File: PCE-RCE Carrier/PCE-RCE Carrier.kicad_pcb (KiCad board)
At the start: 2 copper layers, 38 x 39.5 mm, 52 parts, among them J1 TBL002A-350-08GY-2GY, J10 Conn_01x06_Pin, J11 XT30PW-M, J2 XT60PW-F, J4 XT60PW-F, J5 DF40C-34DP-0.4V_58_, J6 PRT-16766, J7 DF40C-34DP-0.4V_58_, J9 XT30PW-M, Q1 2SD2537, Q2 2SD2537, Q3 2SD2537, Q4 2SD2537, U1 TPS75533KTTRG3, U2 TPS54302DDCR, U3 BD6222HFP-TR, U4 LMR51430, U5 BD6222HFP-TR

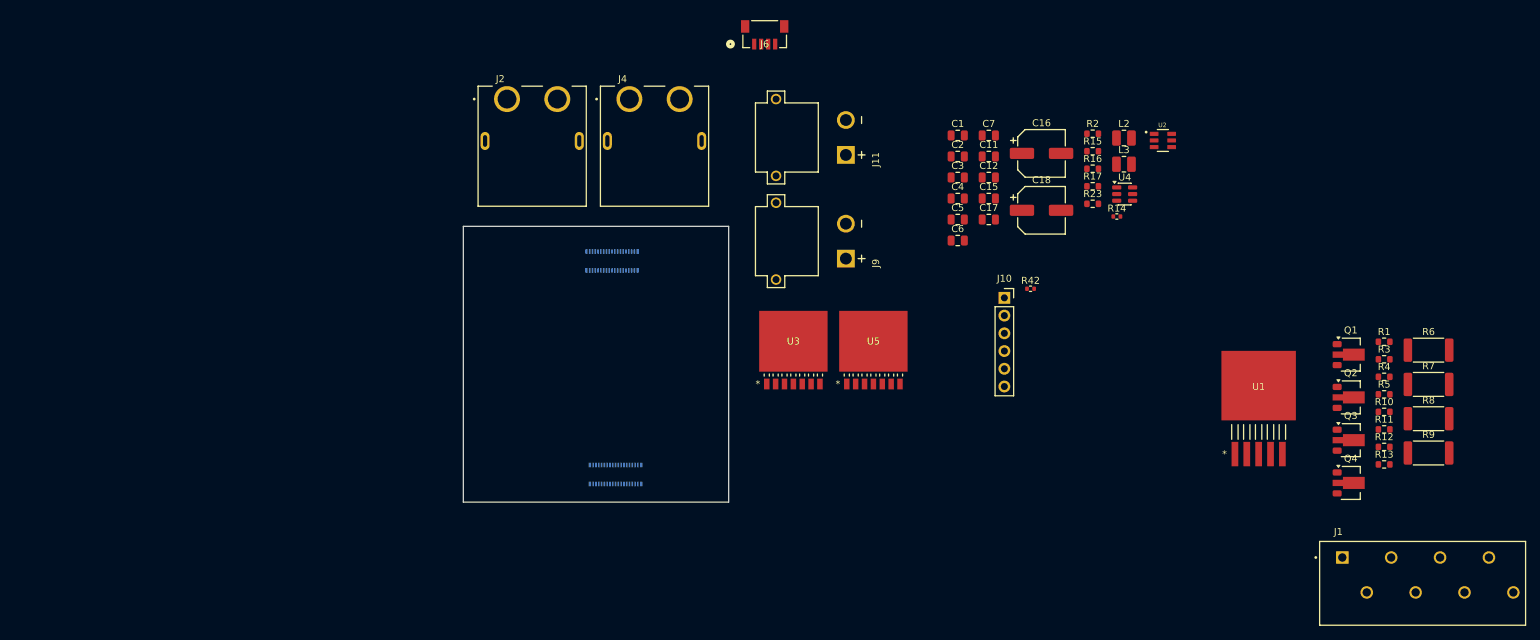
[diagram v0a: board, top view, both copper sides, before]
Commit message: mfw high power components are large
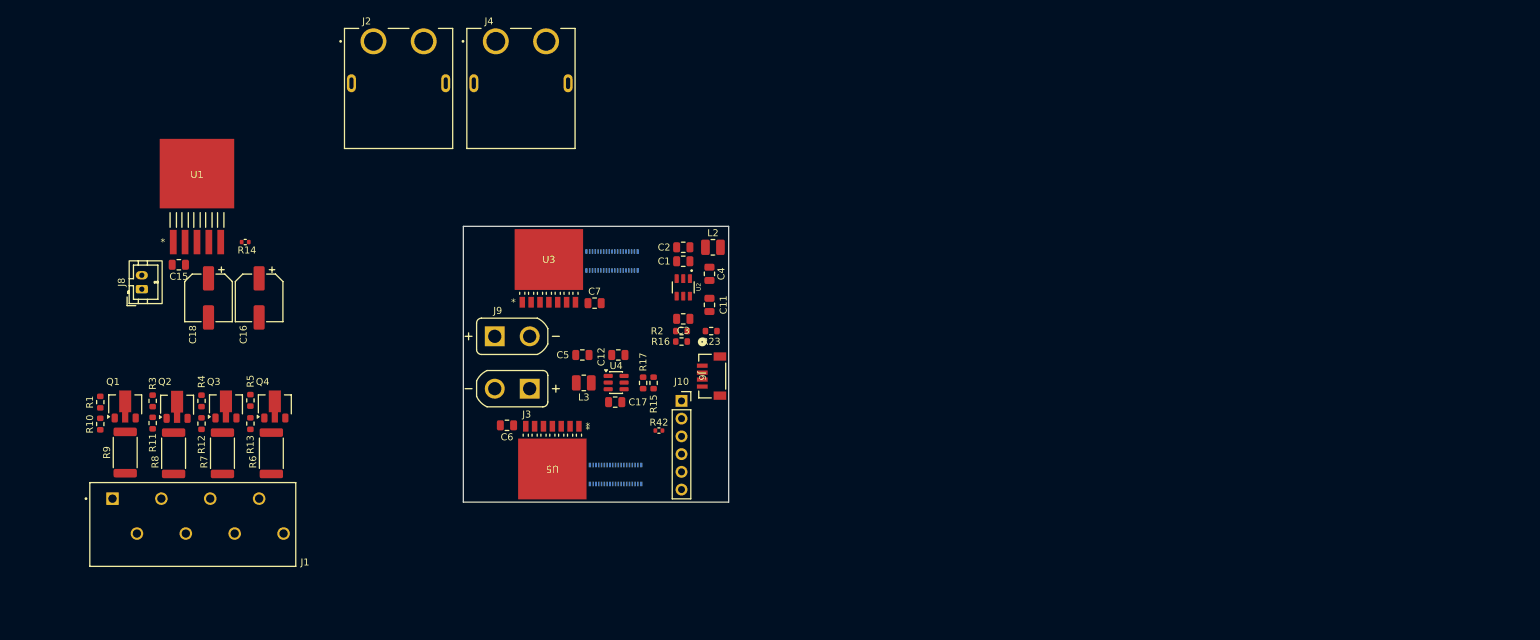
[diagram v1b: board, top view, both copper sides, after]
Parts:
- removed J11: XT30PW-M, XT30PW-M:AMASS_XT30PW-M
- added J3: XT30UPB-M, XT30UPB-M:AMASS_XT30UPB-M, F.Cu at (129.0, 77.2)
- added J8: Conn_01x02_Pin, Connector_JST:JST_PH_B2B-PH-K_1x02_P2.00mm_Vertical, F.Cu at (76.0, 63.0)
- J9: value XT30PW-M -> XT30UPB-M; footprint XT30PW-M:AMASS_XT30PW-M -> XT30UPB-M:AMASS_XT30UPB-M
- moved R9 186.7 mm to (73.6, 86.4), turned to 90 degrees
- moved R1 184.1 mm to (70.0, 79.2), turned to -90 degrees
- moved R10 183.9 mm to (70.0, 82.3), turned to -90 degrees
- moved R8 179.8 mm to (80.5, 86.5), turned to 90 degrees
- moved R3 176.5 mm to (77.5, 79.0), turned to -90 degrees
- moved R11 176.4 mm to (77.5, 82.2), turned to -90 degrees
- moved J1 176.3 mm to (71.8, 93.0)
- moved Q1 175.7 mm to (73.6, 79.5), turned to 90 degrees
- moved R7 173.0 mm to (87.5, 86.5), turned to 90 degrees
- moved R4 169.4 mm to (84.5, 79.0), turned to -90 degrees
- moved R12 169.4 mm to (84.5, 82.2), turned to -90 degrees
- moved Q2 168.1 mm to (81.0, 79.5), turned to 90 degrees
- moved R6 166.4 mm to (94.5, 86.5), turned to 90 degrees
- moved R13 162.5 mm to (91.5, 82.2), turned to -90 degrees
- moved R5 162.4 mm to (91.5, 78.9), turned to -90 degrees
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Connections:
- J10 pad 2: /MOSI -> Net-(J10-Pin_2)
- J10 pad 3: Net-(J10-Pin_3) -> /MOSI
- J9 pad N: /Power Distribution and Motor Control/MOTOR2B -> /Power Distribution and Motor Control/MOTOR1B
- J9 pad P: /Power Distribution and Motor Control/MOTOR2A -> /Power Distribution and Motor Control/MOTOR1A
- R42 pad 2: Net-(J10-Pin_3) -> Net-(J10-Pin_2)

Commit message: initial component placement can you feel the layout hell
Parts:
- moved J4 58.8 mm to (143.7, 84.8)
- moved R1 49.3 mm to (118.7, 87.4), turned to 90 degrees
- moved R10 48.7 mm to (118.7, 84.2), turned to 90 degrees
- moved J2 47.4 mm to (143.2, 63.8), turned to 180 degrees
- moved Q1 42.2 mm to (115.1, 87.0), turned to -90 degrees
- moved R9 42.0 mm to (115.1, 80.2), turned to -90 degrees
- moved R3 34.7 mm to (111.2, 87.5), turned to 90 degrees
- moved U1 34.7 mm to (115.8, 60.2), turned to -90 degrees
- moved R11 33.7 mm to (111.2, 84.4), turned to 90 degrees
- moved R8 28.4 mm to (108.2, 80.0), turned to -90 degrees
- moved Q2 27.7 mm to (107.7, 87.0), turned to -90 degrees
- moved C15 21.7 mm to (102.8, 57.6), turned to 90 degrees
- moved R4 21.4 mm to (104.2, 87.5), turned to 90 degrees
- moved R12 19.8 mm to (104.2, 84.3), turned to 90 degrees
- moved R14 18.8 mm to (106.1, 67.2), turned to 90 degrees
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
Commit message: potentially better placement that was revealed to me in my shower
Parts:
- moved C15 20.7 mm to (82.2, 58.1)
- moved C16 20.7 mm to (77.4, 69.6)
- moved C18 20.7 mm to (77.4, 62.4)
- moved J1 20.7 mm to (60.0, 90.0)
- moved J8 20.7 mm to (70.0, 57.8)
- moved Q1 20.7 mm to (94.4, 87.5)
- moved Q2 20.7 mm to (87.0, 87.5)
- moved Q3 20.7 mm to (80.0, 87.5)
- moved Q4 20.7 mm to (73.0, 87.5)
- moved R1 20.7 mm to (98.0, 87.9)
- moved R10 20.7 mm to (98.0, 84.7)
- moved R11 20.7 mm to (90.5, 84.9)
- moved R12 20.7 mm to (83.5, 84.8)
- moved R13 20.7 mm to (76.5, 84.8)
- moved R14 20.7 mm to (85.4, 67.7)
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
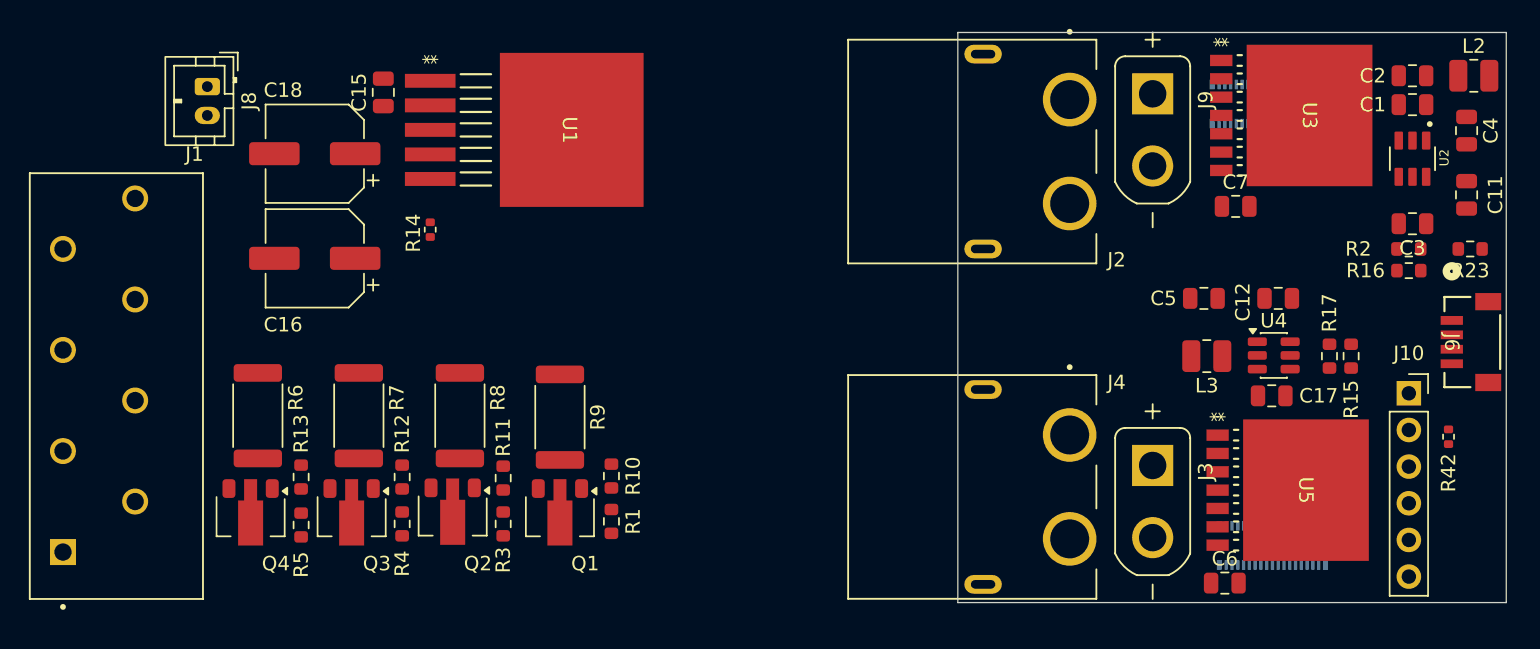
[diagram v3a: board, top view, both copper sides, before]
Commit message: some pce routing, switched out ace battery connectors for vertical xt30
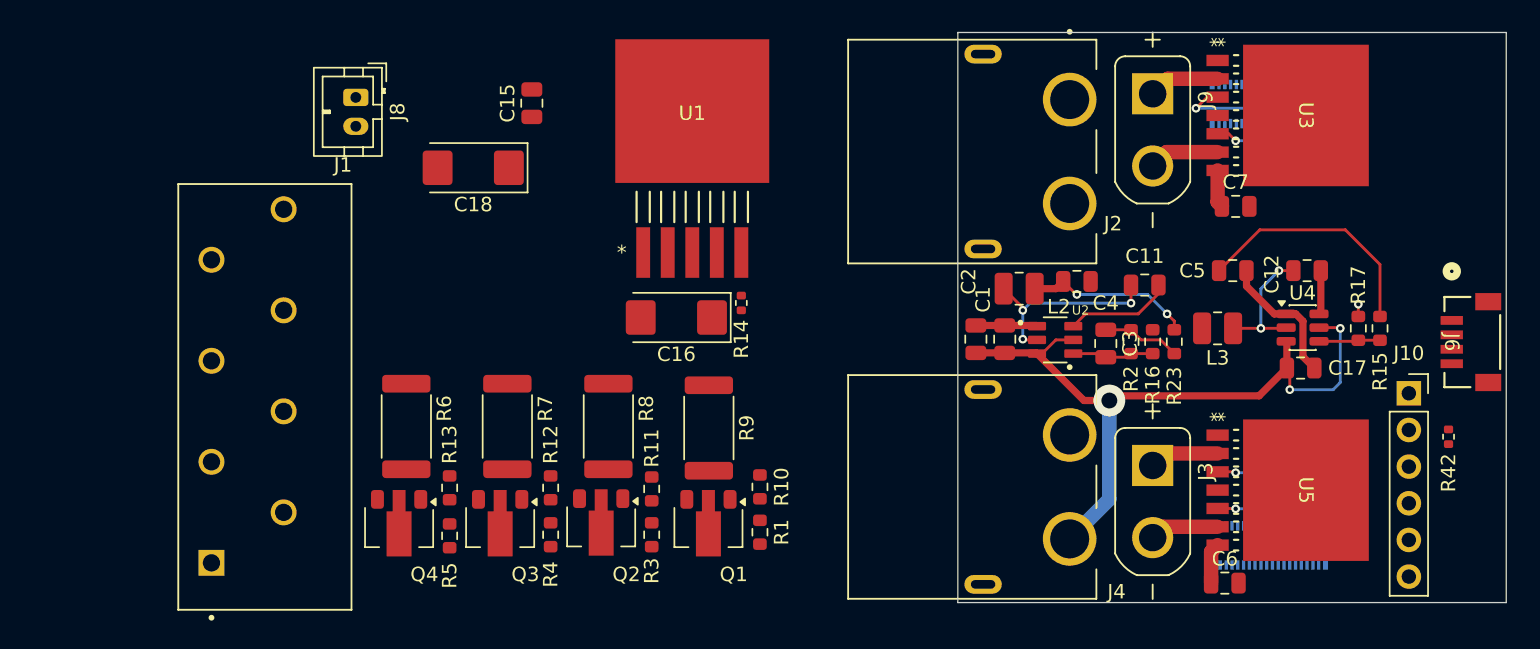
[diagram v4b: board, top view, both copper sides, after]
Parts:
- C16, C18: footprint Capacitor_SMD:CP_Elec_6.3x5.4 -> Capacitor_Tantalum_SMD:CP_EIA-6032-28_Kemet-C
- moved C2 35.3 mm to (123.2, 75.2), turned to 90 degrees
- moved L2 34.8 mm to (126.2, 71.8)
- moved C1 32.6 mm to (125.2, 75.2), turned to 90 degrees
- moved C4 29.0 mm to (130.2, 71.2), turned to 0 degrees
- moved U2 27.8 mm to (128.7, 75.3), turned to 0 degrees
- moved C16 25.4 mm to (102.5, 73.8)
- moved C11 23.2 mm to (134.9, 71.5), turned to 180 degrees
- moved C3 22.8 mm to (132.2, 75.5), turned to -90 degrees
- moved R14 22.1 mm to (107.0, 72.7)
- moved R23 21.5 mm to (137.0, 75.4), turned to 90 degrees
- moved R2 20.3 mm to (134.0, 75.4), turned to 90 degrees
- moved R16 18.4 mm to (135.5, 75.4), turned to -90 degrees
- moved C18 11.0 mm to (88.4, 63.4)
- moved R9 10.3 mm to (104.8, 81.4)
- moved C15 10.3 mm to (92.5, 58.9)
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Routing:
- net VIN: track 0.00 -> 49.9 mm, vias 0 -> 3
- net +12V: track 0.00 -> 22.3 mm
- net GND: track 0.00 -> 14.7 mm, vias 0 -> 1
- net Net-(U2-SW): track 0.00 -> 14.0 mm, vias 0 -> 3
- net +3V3_REG: track 0.00 -> 11.6 mm, vias 0 -> 2
- net Net-(U4-SW): track 0.00 -> 9.21 mm, vias 0 -> 2
- net Net-(U2-BOOT): track 0.00 -> 7.43 mm
- net /PAYLOAD_2F: track 0.00 -> 6.97 mm, vias 0 -> 1
- net /PAYLOAD_1F: track 0.00 -> 6.59 mm, vias 0 -> 1
- net Net-(U2-FB): track 0.00 -> 5.71 mm
- net Net-(C3-Pad1): track 0.00 -> 5.43 mm
- net /PAYLOAD_2R: track 0.00 -> 5.42 mm, vias 0 -> 1
- net /Power Distribution and Motor Control/MOTOR1A: track 0.00 -> 4.93 mm
- net /Power Distribution and Motor Control/MOTOR1B: track 0.00 -> 4.90 mm
- net /Power Distribution and Motor Control/MOTOR2A: track 0.00 -> 4.84 mm
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
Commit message: updated pyro circuit to be like easymini, lowk will prob make it a separate carrier
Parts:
- removed Q1, Q2, Q3, Q4: 2SD2537, Package_TO_SOT_SMD:SOT-89-3
- added C10: 2.2u, Capacitor_SMD:C_0805_2012Metric, F.Cu at (157.8, 64.5)
- added C8: 100n, Capacitor_SMD:C_0402_1005Metric, F.Cu at (102.0, 70.6)
- added C9: 100n, Capacitor_SMD:C_0402_1005Metric, F.Cu at (85.2, 71.9)
- added D1: SM4004, Diode_SMD:D_MELF, F.Cu at (155.5, 60.0)
- added J11: Conn_01x02, Connector_PinSocket_2.54mm:PinSocket_1x02_P2.54mm_Vertical, F.Cu at (157.8, 56.2)
- added Q5: SI7232DN-T1-GE3, Si7232DN:TRANS_SI7232DN-T1-GE3, F.Cu at (99.0, 76.4)
- added Q6: SI7232DN-T1-GE3, Si7232DN:TRANS_SI7232DN-T1-GE3, F.Cu at (94.1, 76.4)
- added R18: 1k, Resistor_SMD:R_0402_1005Metric, F.Cu at (157.2, 62.8)
- added R19: 1M, Resistor_SMD:R_0402_1005Metric, F.Cu at (152.5, 62.8)
- added R20: 100, Resistor_SMD:R_0603_1608Metric, F.Cu at (100.0, 72.5)
- added R21: 100, Resistor_SMD:R_0603_1608Metric, F.Cu at (97.5, 72.5)
- added R22: 100, Resistor_SMD:R_0603_1608Metric, F.Cu at (95.0, 72.5)
- added R24: 100, Resistor_SMD:R_0603_1608Metric, F.Cu at (92.8, 72.5)
- added R25: 10k 1%, Resistor_SMD:R_0402_1005Metric, F.Cu at (90.2, 79.1)
- added R26: 8.06k 1%, Resistor_SMD:R_0402_1005Metric, F.Cu at (88.4, 79.6)
- added R27: 10k 1%, Resistor_SMD:R_0402_1005Metric, F.Cu at (85.4, 79.1)
- added R28: 9.09k 1%, Resistor_SMD:R_0402_1005Metric, F.Cu at (87.2, 79.6)
- added R29: 10k 1%, Resistor_SMD:R_0402_1005Metric, F.Cu at (90.9, 69.9)
- added R30: 8.06k 1%, Resistor_SMD:R_0402_1005Metric, F.Cu at (89.2, 69.4)
- added R31: 10k 1%, Resistor_SMD:R_0402_1005Metric, F.Cu at (86.2, 69.9)
- added R32: 9.09k 1%, Resistor_SMD:R_0402_1005Metric, F.Cu at (87.9, 69.4)
- added U6: LM293, Package_SO:VSSOP-8_3x3mm_P0.65mm, F.Cu at (104.5, 73.1)
- added U7: LM293, Package_SO:VSSOP-8_3x3mm_P0.65mm, F.Cu at (87.8, 74.5)
- R1: value 1k -> 3.3k
- R10, R12: value 220 -> 10k 1%; footprint Resistor_SMD:R_0603_1608Metric -> Resistor_SMD:R_0402_1005Metric
- R11: value 220 -> 8.06k 1%; footprint Resistor_SMD:R_0603_1608Metric -> Resistor_SMD:R_0402_1005Metric
- R13: value 220 -> 9.09k 1%; footprint Resistor_SMD:R_0603_1608Metric -> Resistor_SMD:R_0402_1005Metric
- R6, R9: value 3.3 -> 10k 1%; footprint Resistor_SMD:R_2512_6332Metric -> Resistor_SMD:R_0402_1005Metric
- R7: value 3.3 -> 8.06k 1%; footprint Resistor_SMD:R_2512_6332Metric -> Resistor_SMD:R_0402_1005Metric
- R8: value 3.3 -> 9.09k 1%; footprint Resistor_SMD:R_2512_6332Metric -> Resistor_SMD:R_0402_1005Metric
- moved J1 37.0 mm to (107.2, 91.0), turned to 180 degrees
- moved R13 24.3 mm to (104.0, 68.4), turned to 180 degrees
- moved R5 22.4 mm to (97.5, 69.2)
- moved R12 21.8 mm to (104.5, 66.6)
- moved R6 21.3 mm to (105.0, 79.6), turned to 90 degrees
- moved R1 21.1 mm to (100.0, 69.2)
- moved R3 20.4 mm to (95.0, 69.2)
- moved R4 19.5 mm to (92.8, 69.3)
- moved R10 19.0 mm to (105.8, 66.6)
- moved C16 18.4 mm to (87.2, 63.5), turned to -90 degrees
- moved R11 18.1 mm to (106.3, 68.4), turned to 0 degrees
- moved R7 15.1 mm to (105.5, 77.9), turned to 0 degrees
- moved R14 11.9 mm to (97.5, 65.5), turned to 0 degrees
- moved J8 7.90 mm to (88.0, 56.8), turned to 180 degrees
- moved R8 6.47 mm to (103.3, 77.9), turned to 180 degrees
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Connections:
- C15 pad 1: /Power Distribution and Motor Control/3V7_LIPO -> +3V7_LIPO
- J5 pad 2: /PAYLOAD_A -> unconnected-(J5-Pad2)
- J5 pad 28: unconnected-(J5-Pad28) -> /PAYLOAD_A
- J8 pad 1: /Power Distribution and Motor Control/3V7_LIPO -> +3V7_LIPO
- R1 pad 1: GND -> /PYRO_1
- R1 pad 2: Net-(Q1-Pad1) -> GND
- R10 pad 1: Net-(Q1-Pad1) -> +3V7_LIPO
- R10 pad 2: /PYRO_1 -> Net-(U6B-+)
- R11 pad 1: Net-(Q2-Pad1) -> Net-(U6B-+)
- R11 pad 2: /PYRO_2 -> GND
- R12 pad 1: Net-(Q3-Pad1) -> +3.3V/BP
- R12 pad 2: /PYRO_3 -> Net-(U6B--)
- R13 pad 1: Net-(Q4-Pad1) -> Net-(U6B--)
- R13 pad 2: /PYRO_4 -> GND
- R3 pad 1: GND -> /PYRO_3
- R3 pad 2: Net-(Q2-Pad1) -> GND
- R4 pad 1: GND -> /PYRO_4
- R4 pad 2: Net-(Q3-Pad1) -> GND
- R5 pad 1: GND -> /PYRO_2
- R5 pad 2: Net-(Q4-Pad1) -> GND
- R6 pad 1: Net-(J1-Pad7) -> +3V7_LIPO
- R6 pad 2: Net-(Q4-Pad2) -> Net-(U6A-+)
- R7 pad 1: Net-(J1-Pad5) -> Net-(U6A-+)
- R7 pad 2: Net-(Q3-Pad2) -> GND
- R8 pad 1: Net-(J1-Pad3) -> Net-(U6A--)
- R8 pad 2: Net-(Q2-Pad2) -> GND
- R9 pad 1: Net-(J1-Pad1) -> +3.3V/BP
- R9 pad 2: Net-(Q1-Pad2) -> Net-(U6A--)
- U1 pad 2: /Power Distribution and Motor Control/3V7_LIPO -> +3V7_LIPO
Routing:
- net /PAYLOAD_A: track 0.00 -> 11.5 mm, vias 0 -> 1
- net Net-(D1-A): track 0.00 -> 6.61 mm
- net GND: track 14.7 -> 15.4 mm, vias 1 -> 2
